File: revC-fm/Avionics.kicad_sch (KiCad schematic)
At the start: 76 parts, among them J1 5031821852, P2 TSM-105-01-F-SV, P3 FTSH-105-01-F-DV-K-TR, SW1 KMR231NG LFS, SW2 KMR231NG LFS, U4 MAX708RESA-T, U45 DS1343D-33+, U5 imu-stamp-revA, U6 SN74LVC1T45DCK, U7 MR25H40MDF, U8 ATSAMD51N20A-AUT, Y1 32.768kHz, Y2 32.768kHz

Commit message: teardrops
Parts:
- BT1: value 2998 -> 1056TR; footprint SierraLobo:BatteryHolder_Keystone_2998_1x6.8mm -> SierraLobo:Keystone_1056; Mfr. Part No 2998 -> 1056TR
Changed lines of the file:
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@@
       (effects (font (size 1.27 1.27)) (justify left))
     )
-    (property "Value" "2998" (at 267.97 148.463 0)
+    (property "Value" "1056TR" (at 267.97 148.463 0)
       (effects (font (size 1.27 1.27)) (justify left))
     )
-    (property "Footprint" "SierraLobo:BatteryHolder_Keystone_2998_1x6.8mm" (at 264.16 147.066 90)
+    (property "Footprint" "SierraLobo:Keystone_1056" (at 264.16 147.066 90)
       (effects (font (size 1.27 1.27)) hide)
     )
@@
       (effects (font (size 1.27 1.27)) hide)
     )
-    (property "Mfr. Part No" "2998" (at 264.16 148.59 0)
+    (property "Mfr. Part No" "1056TR" (at 264.16 148.59 0)
       (effects (font (size 1.27 1.27)) hide)
     )

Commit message: working revC review changes
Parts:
- renumbered C137 to C30, C30 to C31, C31 to C32, C32 to C33, C33 to C34, C34 to C35, LED2 to LED1, LED1 to LED2, LED4 to LED3, LED3 to LED4, R11 to R10, R14 to R11, R16 to R12, R10 to R13, R12 to R14, R13 to R15, R15 to R16, R20 to R18, R18 to R19, R19 to R20, R268 to R24, R24 to R25, R25 to R26, R271 to R27, R26 to R28, R27 to R29, R28 to R30, R29 to R31, U5 to U4, U4 to U5, U45 to U9
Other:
- moved on the sheet: SW2

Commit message: working revC
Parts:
- removed C27, C29, C31, C32, C33, C34: 0.1uF, Capacitor_SMD:C_0603_1608Metric, symbol Device:C
- removed LED1, LED2, LED3, LED4: SK68xx-EC3210x, SierraLobo:LED_SK68xx-EC3210x, symbol SierraLobo:SK68xx-EC3210x
- removed R15: 470k, Resistor_SMD:R_0603_1608Metric, symbol Device:R_US
- removed R17: 39k, Resistor_SMD:R_0603_1608Metric, symbol Device:R_US
- removed R19, R22, R23, R28, R29: 1k, Resistor_SMD:R_0603_1608Metric, symbol Device:R_US
- removed U6: SN74LVC1T45DCK, Package_TO_SOT_SMD:SOT-363_SC-70-6, symbol Logic_LevelTranslator:SN74LVC1T45DCK
- added BOMTIE1: BR1220, symbol SierraLobo:BOMTIE
- added R243, R244: 1k, Resistor_SMD:R_0402_1005Metric, symbol Device:R_US
- C10, C11, C26, C4, C5, C6, C7, C8, C9: footprint Capacitor_SMD:C_0603_1608Metric -> Capacitor_SMD:C_0402_1005Metric
- C17, C18, C23, C25: Mfr. Part No (none) -> CGA4J1X7S1E106K125AE
- C27: renamed from C28; footprint Capacitor_SMD:C_0603_1608Metric -> Capacitor_SMD:C_0402_1005Metric
- C29: renamed from C30; footprint Capacitor_SMD:C_0603_1608Metric -> Capacitor_SMD:C_0402_1005Metric
- C47, C48: Mfr. Part No (none) -> C3216X5R1E476M160AC
- L1: Mfr. Part No (none) -> BCL322520RT-100M-D
- P2: Mfr. Part No (none) -> TSM-105-01-F-SV
- P3: Mfr. Part No (none) -> FTSH-105-01-F-DV-K-TR
- R11: value 1k -> 10k; footprint Resistor_SMD:R_0603_1608Metric -> Resistor_SMD:R_0402_1005Metric
- R14, R7, R8: footprint Resistor_SMD:R_0603_1608Metric -> Resistor_SMD:R_0402_1005Metric
- R16: renamed from R18; footprint Resistor_SMD:R_0603_1608Metric -> Resistor_SMD:R_0402_1005Metric
- R18: renamed from R20; footprint Resistor_SMD:R_0603_1608Metric -> Resistor_SMD:R_0402_1005Metric
- R19: renamed from R21; footprint Resistor_SMD:R_0603_1608Metric -> Resistor_SMD:R_0402_1005Metric
- R22: renamed from R24; footprint Resistor_SMD:R_0603_1608Metric -> Resistor_SMD:R_0402_1005Metric
- R25: renamed from R27; footprint Resistor_SMD:R_0603_1608Metric -> Resistor_SMD:R_0402_1005Metric
- R28: renamed from R30; footprint Resistor_SMD:R_0603_1608Metric -> Resistor_SMD:R_0402_1005Metric
- U5: Mfr. Part No (none) -> MAX708RESA-T
- U7: Mfr. Part No (none) -> MR25H40MDF
- U8: Mfr. Part No (none) -> ATSAMD51N20A-AUT
- U9: Mfr. Part No DS1344D-33+ -> DS1343D-33+
- Y1: Mfr. Part No (none) -> ABS07AIG-32.768KHZ-1-T
- renumbered C35 to C34, R16 to R15, R25 to R23, R26 to R24, R31 to R29
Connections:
- net SOLAR is gone; now on net CHRG_SHDN: U8.20 (PA07)
- net CHRG_SHDN: no longer U8.70 (PA20)
- net NeoPixel_DIN: now reaches U8.71 (PA21)
- net CHRG_STAT: no longer names the net of U8.55 (PA19)
- net CHRG_STAT: now also R243.1
- new net: R244.1, U8.70 (PA20)
- new net CHRG_1: R243.2
- new net CHRG_2: R244.2
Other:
- note added: "12.5mm coin cell holder"
- note added: "IMU devices address prog"
- note added: "Real Time Clock"
- note added: "SELF TEST"
- note removed: "6.8mm coin cell"
- note removed: "RTC"
- moved on the sheet: BT1, C10, C11, C12, C13, C14, C15, C16, C17, C18, C21, C22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

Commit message: working
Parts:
- renumbered C27 to C25, C29 to C27, C25 to C28, C34 to C29, R8 to R10, R9 to R11, R18 to R12, R15 to R14, R243 to R15, R244 to R16, R22 to R17, R14 to R18, R25 to R20, R16 to R21, R24 to R22, R10 to R24, R11 to R25, R12 to R26, R28 to R27, R29 to R28, R7 to R9, SW1 to SW2, SW2 to SW3, U7 to U4, U9 to U5, U5 to U6, U8 to U7, U4 to U8

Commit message: updated fab files
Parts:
- BT1: Manufacturer (none) -> Keystone Electronics
- C10, C11, C25, C26, C27, C4, C5, C6, C7, C8, C9: Manufacturer (none) -> TDK; Mfr. Part No (none) -> CGA2B3X7R1H104K050BE
- C12, C13, C14, C15, C16, C22, C29: Manufacturer (none) -> TDK; Mfr. Part No (none) -> CGA3E1X7R1V105K080AE
- C17, C18, C23, C28, C47, C48, L1: Manufacturer (none) -> TDK
- C21, C24: Manufacturer (none) -> TDK; Mfr. Part No (none) -> CGA2B2NP01H080D050BA
- J1: Manufacturer (none) -> Molex; Mfr. Part No (none) -> 5031821852
- P2, P3: Manufacturer (none) -> Samtec
- R10, R12, R17, R18, R19, R20, R21, R25, R27, R9: Manufacturer (none) -> Stackpole Electronics; Mfr. Part No (none) -> RMCF0402FT10K0
- R11, R28: Manufacturer (none) -> Stackpole Electronics; Mfr. Part No (none) -> RMCF0603FT330R
- R13: Manufacturer (none) -> Stackpole Electronics; Mfr. Part No (none) -> RMCF0603FT316K
- R14: Manufacturer (none) -> Stackpole Electronics; Mfr. Part No (none) -> RMCF0603FT110K
- R15, R16: Manufacturer (none) -> Panasonic; Mfr. Part No (none) -> ERJ-2GEJ102X
- R22, R23: Manufacturer (none) -> Stackpole Electronics; Mfr. Part No (none) -> RMCF0603FT2K70
- R24: Manufacturer (none) -> Stackpole Electronics; Mfr. Part No (none) -> RMCF0603FT976K
- R26: Manufacturer (none) -> Stackpole Electronics; Mfr. Part No (none) -> RMCF0603FG102K
- SW2, SW3: Manufacturer (none) -> C&K; Mfr. Part No (none) -> KMR231NG LFS
- U4: Manufacturer (none) -> Everspin Technologies
- U5, U6: Manufacturer (none) -> Analog Devices/Maxim Integrated
- U7: Manufacturer (none) -> Microchip Technology
- U8: Manufacturer (none) -> Sierra Lobo
- Y1, Y2: Manufacturer (none) -> Abracon
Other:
- note removed: "DOUBLE CHECK DIVIDERS"

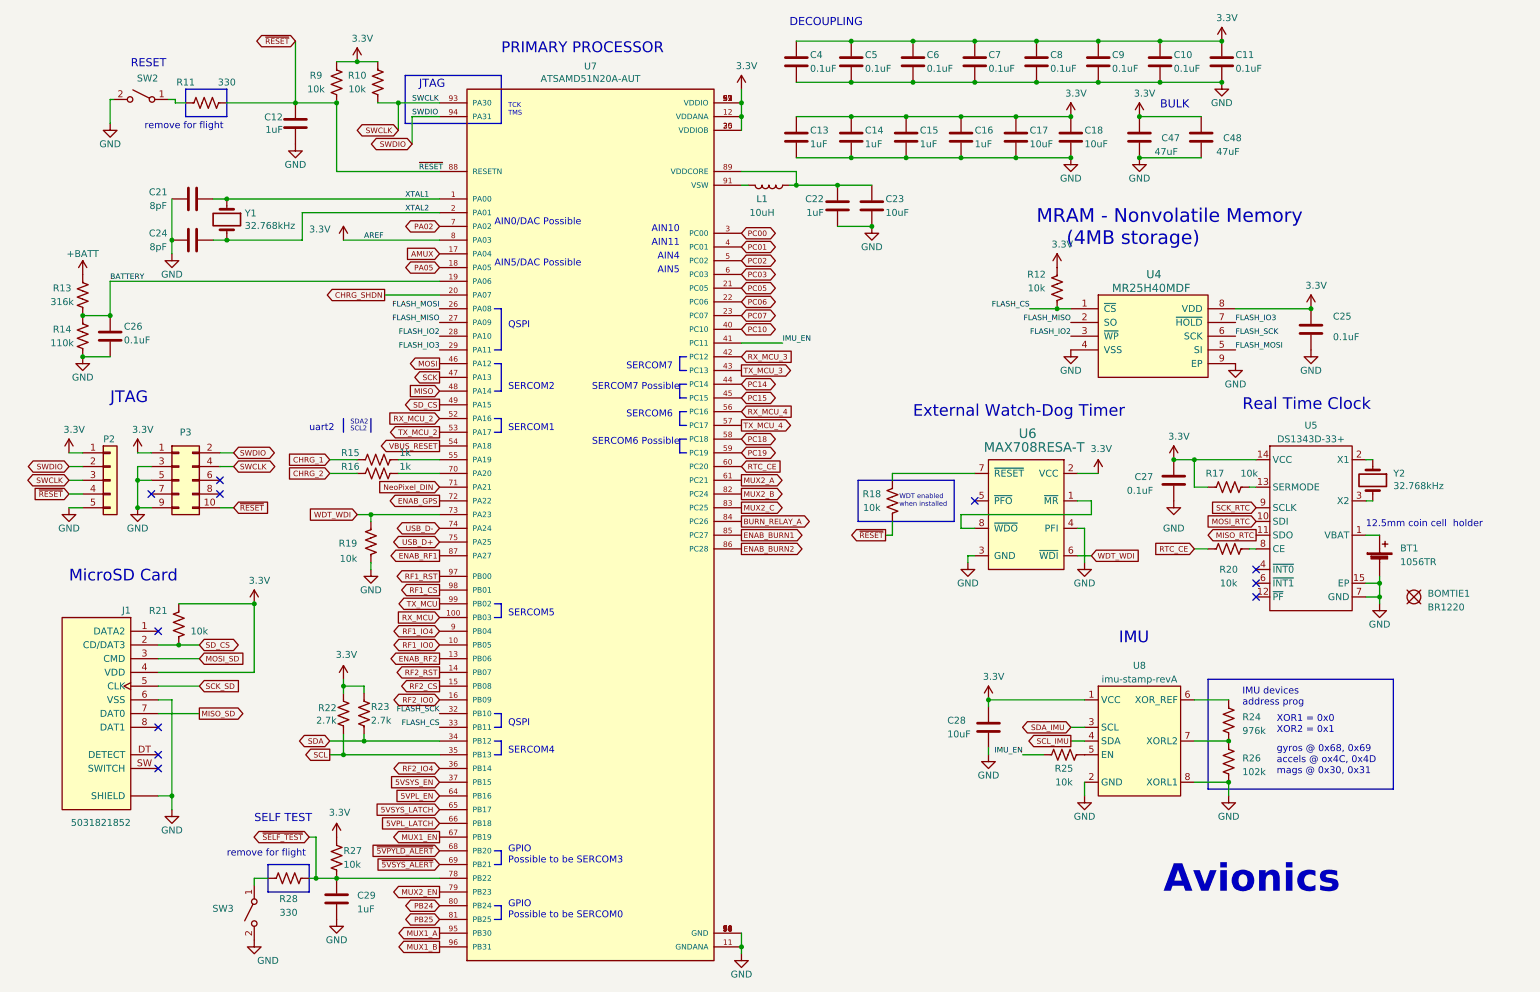
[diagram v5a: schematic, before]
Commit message: updated per review, improved docs
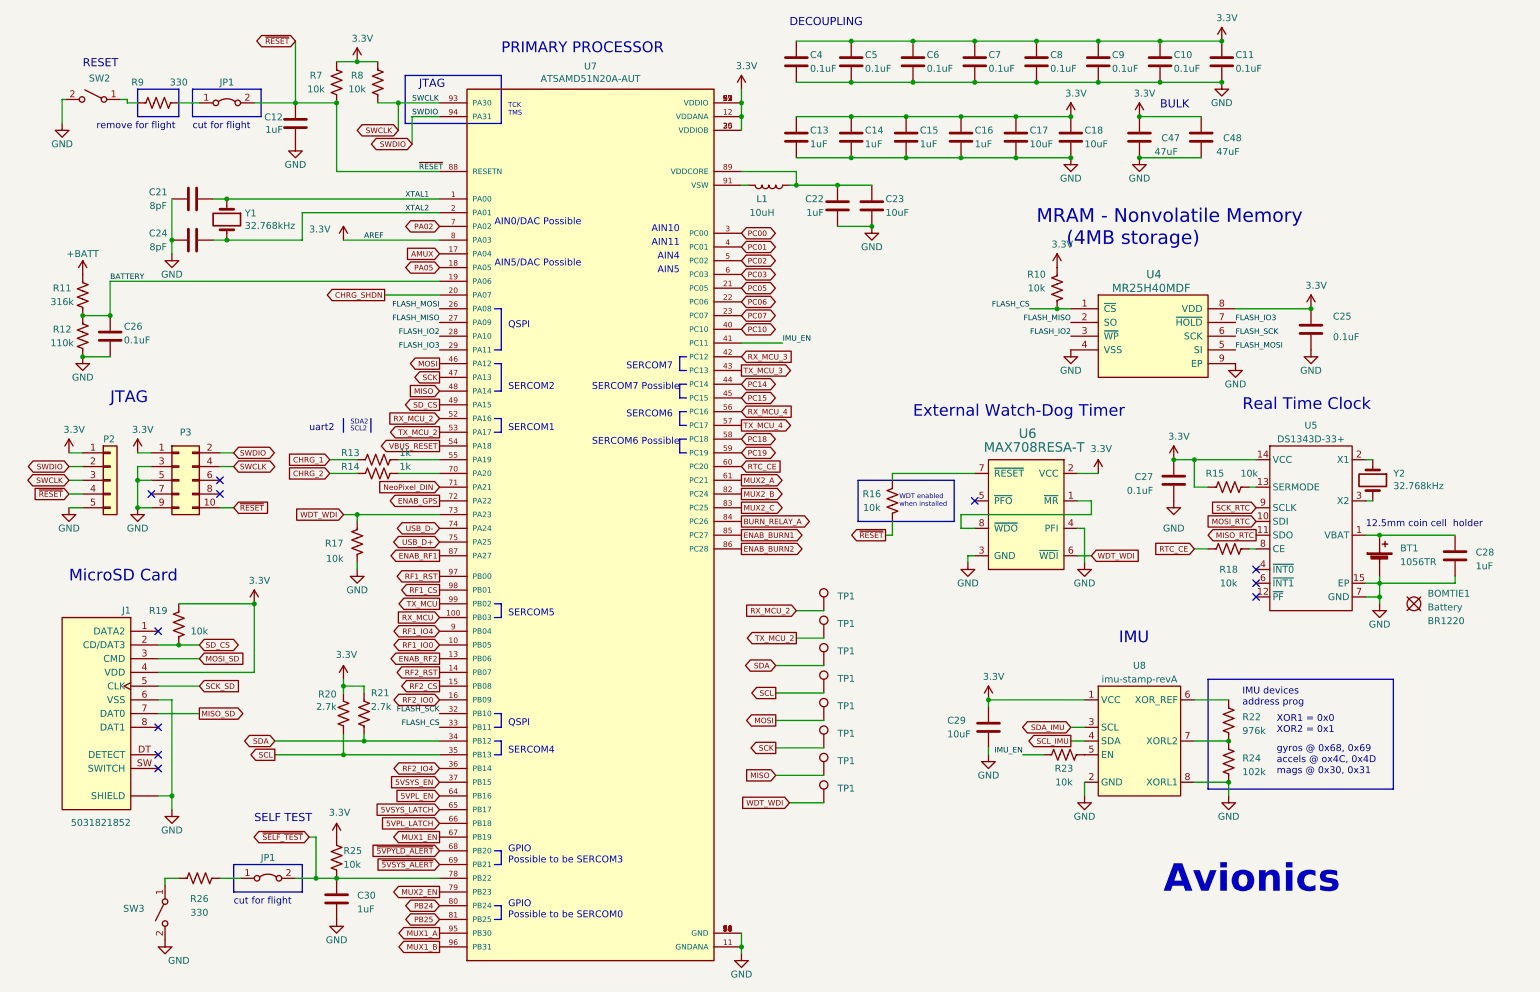
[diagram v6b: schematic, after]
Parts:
- added C28: 1uF, Capacitor_SMD:C_0603_1608Metric, symbol Device:C
- added JP1 (x2): Wire Cut Jumper, Resistor_SMD:R_0603_1608Metric, symbol Jumper:Jumper_2_Bridged
- added TP1 (x8): RCU-0C, SierraLobo:TestPoint_TE_RCU_0603, symbol Connector:TestPoint
- BOMTIE1: value BR1220 -> Battery; Manufacturer (none) -> Panasoic; Mfr. Part No (none) -> BR1220
- renumbered C28 to C29, C29 to C30, R12 to R10, R13 to R11, R14 to R12, R15 to R13, R16 to R14, R17 to R15, R18 to R16, R19 to R17, R20 to R18, R21 to R19, R22 to R20, R23 to R21, R24 to R22, R25 to R23, R26 to R24, R27 to R25, R28 to R26, R9 to R7, R10 to R8, R11 to R9
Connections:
- net GND: now also C28.2
- net MISO: now also TP1.1
- net MOSI: now also TP1.1
- net RX_MCU_2: now also TP1.1
- net SCK: now also TP1.1
- net SCL: now also TP1.1
- net SDA: now also TP1.1
- net TX_MCU_2: now also TP1.1
- net WDT_WDI: now also TP1.1
- net ~{RESET}: now also JP1.2 (B); no longer R9.2
- net ~{SELF_TEST}: now also JP1.2 (B); no longer R26.2
- net at BT1.1 (+), U5.1 (VBAT): now also C28.1
- new net: JP1.1 (A), R9.2
- new net: JP1.1 (A), R26.2
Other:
- note added: "cut for flight"
- moved on the sheet: BOMTIE1, R17, R26, R9, SW2, SW3
